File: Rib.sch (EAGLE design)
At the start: 34 parts, among them IC1 REG1117, IC2 REG1117, X1 JST-XH-03-PIN-LONG-PAD, X2 JST-XH-03-PIN-LONG-PAD

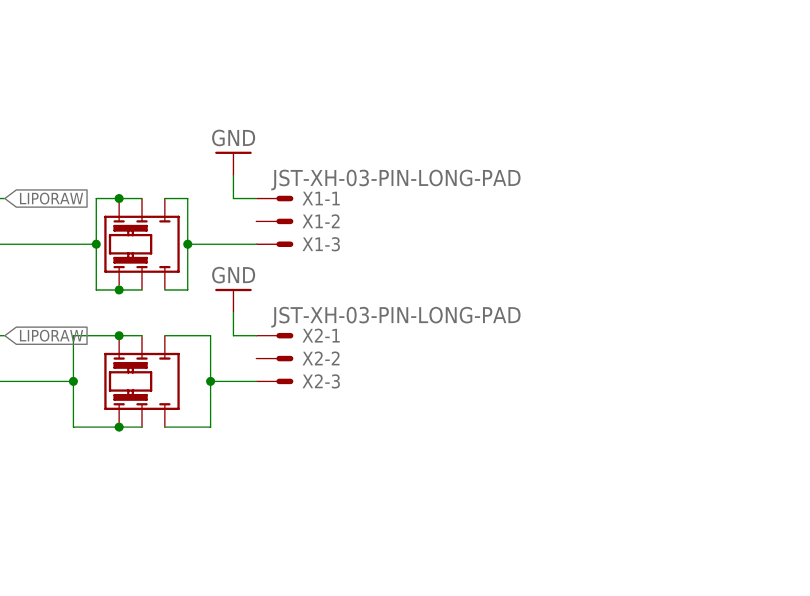
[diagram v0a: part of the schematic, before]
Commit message: Replaced JST power connectors with screw terminals
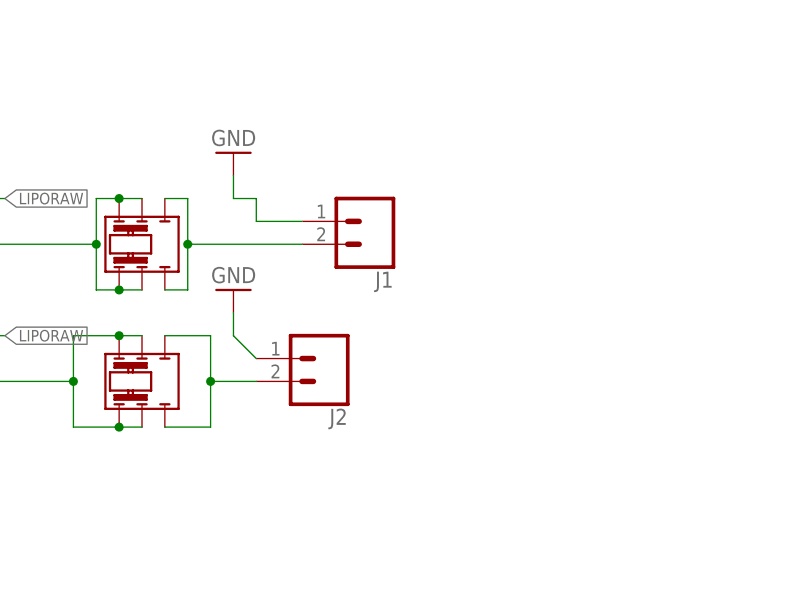
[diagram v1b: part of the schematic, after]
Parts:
- removed X1, X2: JST-XH-03-PIN-LONG-PAD, Rembrandt Electronics - JST XH Connectors v1-0:JST-XH-03-PIN-LONG-PAD
- added J1, J2: (no value), SparkFun-Connectors:CONN_023.5MM_LOCK
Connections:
- net GND: now also J1.1, J2.1; no longer X1-1.S, X2-1.S
- net N$11: now also J1.2; no longer X1-3.S
- net N$39: now also J2.2; no longer X2-3.S
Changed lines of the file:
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@@
 <part name="JP6" library="headers" deviceset="PINHD-1X19" device=""/>
 <part name="JP7" library="headers" deviceset="PINHD-1X19" device=""/>
-<part name="X1" library="Rembrandt Electronics - JST XH Connectors v1-0" deviceset="JST-XH-03-PIN" device="-LONG-PAD"/>
 <part name="JP2" library="headers" deviceset="PINHD-1X19" device=""/>
 <part name="JP8" library="headers" deviceset="PINHD-1X19" device=""/>
@@
 <part name="GND1" library="supply1" library_urn="urn:adsk.eagle:library:371" deviceset="GND" device=""/>
 <part name="GND2" library="supply1" library_urn="urn:adsk.eagle:library:371" deviceset="GND" device=""/>
-<part name="X2" library="Rembrandt Electronics - JST XH Connectors v1-0" deviceset="JST-XH-03-PIN" device="-LONG-PAD"/>
 <part name="U$3" library="wiichuck" deviceset="WIICHUCK" device=""/>
 <part name="U$5" library="wiichuck" deviceset="WIICHUCK" device=""/>
@@
 <part name="U$1" library="GF-126-0327" deviceset="DPDT" device=""/>
 <part name="U$2" library="GF-126-0327" deviceset="DPDT" device=""/>
+<part name="J1" library="SparkFun-Connectors" deviceset="CONN_02" device="3.5MM_LOCK"/>
+<part name="J2" library="SparkFun-Connectors" deviceset="CONN_02" device="3.5MM_LOCK"/>
 </parts>
 <sheets>
@@
 <instance part="JP6" gate="G$1" x="-55.88" y="-170.18"/>
 <instance part="JP7" gate="G$1" x="-35.56" y="-170.18"/>
-<instance part="X1" gate="-1" x="76.2" y="-55.88"/>
-<instance part="X1" gate="-2" x="76.2" y="-58.42"/>
-<instance part="X1" gate="-3" x="76.2" y="-60.96"/>
 <instance part="JP2" gate="G$1" x="-76.2" y="-170.18"/>
 <instance part="JP8" gate="G$1" x="-27.94" y="-170.18"/>
@@
 <instance part="GND1" gate="1" x="-35.56" y="-274.32"/>
 <instance part="GND2" gate="1" x="-22.86" y="-274.32"/>
-<instance part="X2" gate="-1" x="76.2" y="-71.12"/>
-<instance part="X2" gate="-2" x="76.2" y="-73.66"/>
-<instance part="X2" gate="-3" x="76.2" y="-76.2"/>
 <instance part="U$3" gate="G$1" x="38.1" y="-144.78"/>
 <instance part="U$5" gate="G$1" x="38.1" y="-180.34"/>
@@
 <instance part="U$1" gate="G$1" x="68.58" y="-53.34" rot="R90"/>
 <instance part="U$2" gate="G$1" x="68.58" y="-68.58" rot="R90"/>
+<instance part="J1" gate="G$1" x="86.36" y="-58.42" rot="R180"/>
+<instance part="J2" gate="G$1" x="81.28" y="-73.66" rot="R180"/>
 </instances>
 <busses>
@@
 <pinref part="GND10" gate="1" pin="GND"/>
 <wire x1="71.12" y1="-53.34" x2="71.12" y2="-55.88" width="0.1524" layer="91"/>
-<pinref part="X1" gate="-1" pin="S"/>
 <wire x1="71.12" y1="-55.88" x2="73.66" y2="-55.88" width="0.1524" layer="91"/>
+<pinref part="J1" gate="G$1" pin="1"/>
+<wire x1="78.74" y1="-58.42" x2="73.66" y2="-58.42" width="0.1524" layer="91"/>
+<wire x1="73.66" y1="-58.42" x2="73.66" y2="-55.88" width="0.1524" layer="91"/>
 </segment>
 <segment>
 <pinref part="GND9" gate="1" pin="GND"/>
 <wire x1="71.12" y1="-68.58" x2="71.12" y2="-71.12" width="0.1524" layer="91"/>
-<pinref part="X2" gate="-1" pin="S"/>
-<wire x1="71.12" y1="-71.12" x2="73.66" y2="-71.12" width="0.1524" layer="91"/>
+<wire x1="71.12" y1="-71.12" x2="73.66" y2="-73.66" width="0.1524" layer="91"/>
+<pinref part="J2" gate="G$1" pin="1"/>
 </segment>
 <segment>
@@
 <wire x1="66.04" y1="-66.04" x2="66.04" y2="-60.96" width="0.1524" layer="91"/>
 <wire x1="66.04" y1="-60.96" x2="66.04" y2="-55.88" width="0.1524" layer="91"/>
-<pinref part="X1" gate="-3" pin="S"/>
-<wire x1="73.66" y1="-60.96" x2="66.04" y2="-60.96" width="0.1524" layer="91"/>
+<wire x1="78.74" y1="-60.96" x2="66.04" y2="-60.96" width="0.1524" layer="91"/>
 <junction x="66.04" y="-60.96"/>
 <pinref part="U$1" gate="G$1" pin="C2"/>
@@
 <pinref part="U$1" gate="G$1" pin="C1"/>
 <wire x1="66.04" y1="-55.88" x2="63.5" y2="-55.88" width="0.1524" layer="91"/>
+<pinref part="J1" gate="G$1" pin="2"/>
 </segment>
 </net>
@@
 <wire x1="68.58" y1="-71.12" x2="68.58" y2="-76.2" width="0.1524" layer="91"/>
 <wire x1="68.58" y1="-76.2" x2="68.58" y2="-81.28" width="0.1524" layer="91"/>
-<pinref part="X2" gate="-3" pin="S"/>
 <wire x1="73.66" y1="-76.2" x2="68.58" y2="-76.2" width="0.1524" layer="91"/>
 <junction x="68.58" y="-76.2"/>
@@
 <pinref part="U$2" gate="G$1" pin="C1"/>
 <wire x1="63.5" y1="-71.12" x2="68.58" y2="-71.12" width="0.1524" layer="91"/>
-</segment>
-</net>
+<pinref part="J2" gate="G$1" pin="2"/>
+</segment>
+</net>

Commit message: ESP32 SDA now on pin 21
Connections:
- removed net N$38: JP17.14, JP7.14, JP8.14
- new net N$24: JP17.18, JP7.18, JP8.18
- net SDA: now also JP17.14, JP7.14, JP8.14; no longer JP17.18, JP7.18, JP8.18
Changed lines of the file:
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@@
-</segment>
-</net>
-<net name="N$38" class="0">
-<segment>
-<pinref part="JP8" gate="G$1" pin="14"/>
-<pinref part="JP17" gate="G$1" pin="14"/>
-<wire x1="-22.86" y1="-182.88" x2="-30.48" y2="-182.88" width="0.1524" layer="91"/>
-<pinref part="JP7" gate="G$1" pin="14"/>
-<junction x="-30.48" y="-182.88"/>
-<wire x1="-30.48" y1="-182.88" x2="-38.1" y2="-182.88" width="0.1524" layer="91"/>
 </segment>
 </net>
@@
 </segment>
 <segment>
-<pinref part="JP8" gate="G$1" pin="18"/>
-<pinref part="JP17" gate="G$1" pin="18"/>
-<wire x1="-22.86" y1="-193.04" x2="-30.48" y2="-193.04" width="0.1524" layer="91"/>
-<pinref part="JP7" gate="G$1" pin="18"/>
-<junction x="-30.48" y="-193.04"/>
-<wire x1="-30.48" y1="-193.04" x2="-38.1" y2="-193.04" width="0.1524" layer="91"/>
-</segment>
-<segment>
 <pinref part="JP14" gate="A" pin="9"/>
 <pinref part="JP20" gate="A" pin="9"/>
@@
 <wire x1="91.44" y1="-297.18" x2="81.28" y2="-297.18" width="0.1524" layer="91"/>
 <junction x="91.44" y="-297.18"/>
+</segment>
+<segment>
+<pinref part="JP8" gate="G$1" pin="14"/>
+<pinref part="JP17" gate="G$1" pin="14"/>
+<wire x1="-22.86" y1="-182.88" x2="-30.48" y2="-182.88" width="0.1524" layer="91"/>
+<pinref part="JP7" gate="G$1" pin="14"/>
+<junction x="-30.48" y="-182.88"/>
+<wire x1="-30.48" y1="-182.88" x2="-38.1" y2="-182.88" width="0.1524" layer="91"/>
 </segment>
 </net>
@@
 </segment>
 </net>
+<net name="N$24" class="0">
+<segment>
+<pinref part="JP17" gate="G$1" pin="18"/>
+<pinref part="JP8" gate="G$1" pin="18"/>
+<wire x1="-22.86" y1="-193.04" x2="-30.48" y2="-193.04" width="0.1524" layer="91"/>
+<pinref part="JP7" gate="G$1" pin="18"/>
+<wire x1="-30.48" y1="-193.04" x2="-38.1" y2="-193.04" width="0.1524" layer="91"/>
+<junction x="-30.48" y="-193.04"/>
+</segment>
+</net>

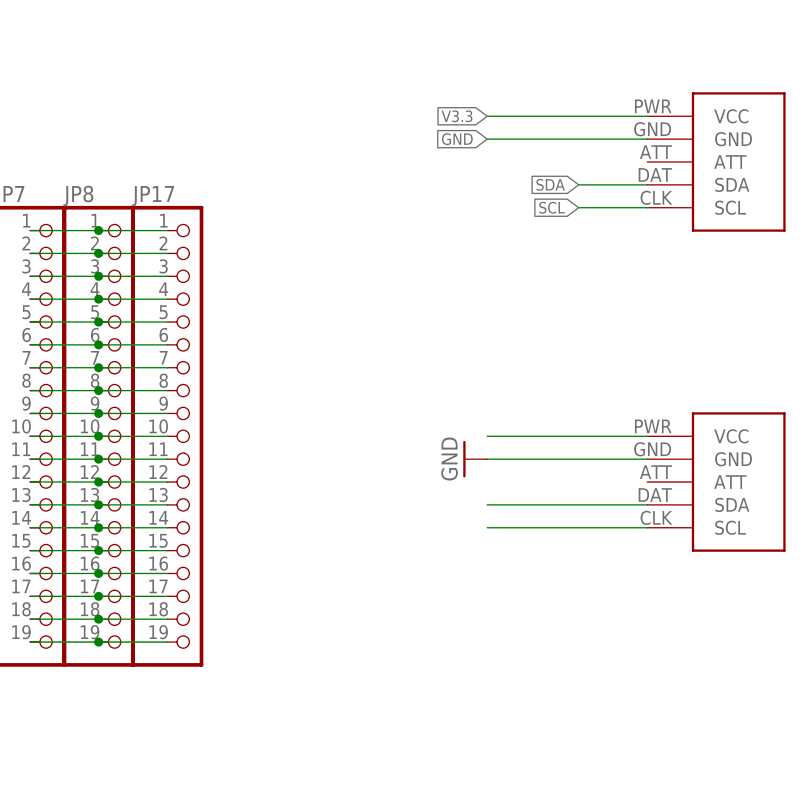
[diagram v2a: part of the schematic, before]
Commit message: DET pins routed to esp and teensy
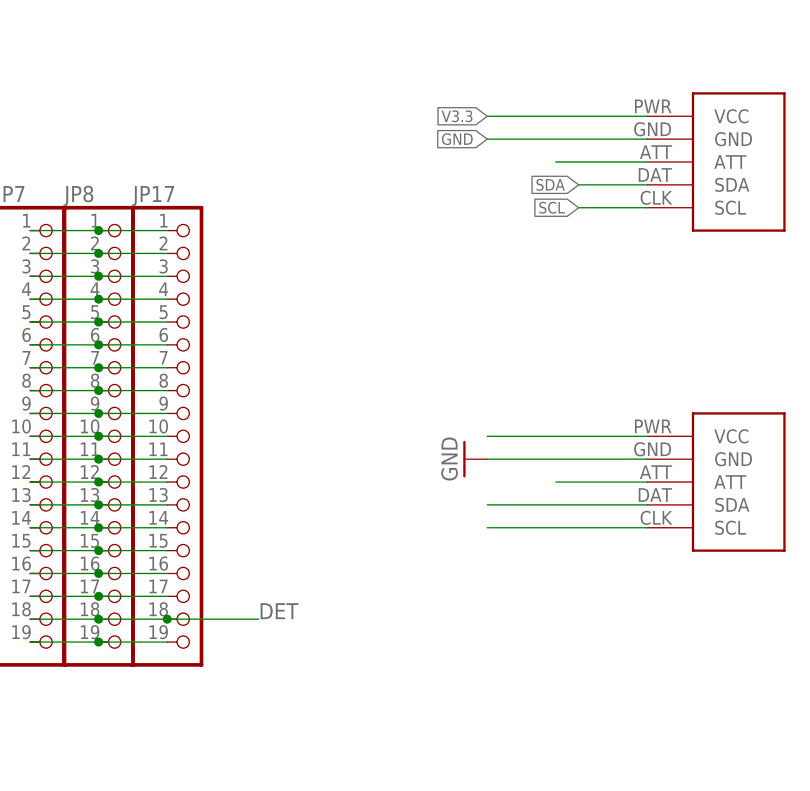
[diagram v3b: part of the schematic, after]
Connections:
- removed net N$107: JP12.24, JP21.24, JP9.24
- removed net N$24: JP17.18, JP7.18, JP8.18
- new net DET: JP12.24, JP17.18, JP21.24, JP7.18, JP8.18, JP9.24, U$3.ATT, U$5.ATT
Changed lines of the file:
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@@
 <?xml version="1.0" encoding="utf-8"?>
 <!DOCTYPE eagle SYSTEM "eagle.dtd">
-<eagle version="8.3.2">
+<eagle version="8.6.3">
 <drawing>
 <settings>
@@
 </segment>
 </net>
-<net name="N$107" class="0">
-<segment>
-<pinref part="JP9" gate="A" pin="24"/>
-<pinref part="JP21" gate="A" pin="24"/>
-<wire x1="119.38" y1="-335.28" x2="132.08" y2="-335.28" width="0.1524" layer="91"/>
-<pinref part="JP12" gate="A" pin="24"/>
-<wire x1="132.08" y1="-335.28" x2="139.7" y2="-335.28" width="0.1524" layer="91"/>
-<junction x="132.08" y="-335.28"/>
-</segment>
-</net>
 <net name="V3.3" class="0">
 <segment>
@@
 </segment>
 </net>
-<net name="N$24" class="0">
+<net name="DET" class="0">
 <segment>
 <pinref part="JP17" gate="G$1" pin="18"/>
@@
 <wire x1="-30.48" y1="-193.04" x2="-38.1" y2="-193.04" width="0.1524" layer="91"/>
 <junction x="-30.48" y="-193.04"/>
-</segment>
-</net>
+<wire x1="-22.86" y1="-193.04" x2="-12.7" y2="-193.04" width="0.1524" layer="91"/>
+<junction x="-22.86" y="-193.04"/>
+<label x="-12.7" y="-193.04" size="1.778" layer="95"/>
+</segment>
+<segment>
+<pinref part="U$3" gate="G$1" pin="ATT"/>
+<wire x1="30.48" y1="-142.24" x2="20.32" y2="-142.24" width="0.1524" layer="91"/>
+</segment>
+<segment>
+<pinref part="U$5" gate="G$1" pin="ATT"/>
+<wire x1="30.48" y1="-177.8" x2="20.32" y2="-177.8" width="0.1524" layer="91"/>
+</segment>
+<segment>
+<pinref part="JP9" gate="A" pin="24"/>
+<pinref part="JP21" gate="A" pin="24"/>
+<wire x1="119.38" y1="-335.28" x2="132.08" y2="-335.28" width="0.1524" layer="91"/>
+<pinref part="JP12" gate="A" pin="24"/>
+<wire x1="132.08" y1="-335.28" x2="139.7" y2="-335.28" width="0.1524" layer="91"/>
+<junction x="132.08" y="-335.28"/>
+</segment>
+</net>

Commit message: Replaced fuseholder with blade style automotive fuse
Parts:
- removed F1, F2: 0154, SMT_Fuse_0154001:0154
- added F3, F4: 3557-2, 3557-2:3557-2
- renumbered U$1 to SW1, U$2 to SW2
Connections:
- net LIPORAW: now also F3.P$2, F4.P$2; no longer F1.P$2, F2.P$2
- net VCC: now also F3.P$1, F4.P$1; no longer F1.P$1, F2.P$1
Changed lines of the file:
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@@
 <layer number="59" name="tCarbon" color="7" fill="1" visible="no" active="no"/>
 <layer number="60" name="bCarbon" color="7" fill="1" visible="no" active="no"/>
+<layer number="88" name="SimResults" color="9" fill="1" visible="yes" active="yes"/>
+<layer number="89" name="SimProbes" color="9" fill="1" visible="yes" active="yes"/>
 <layer number="90" name="Modules" color="5" fill="1" visible="yes" active="yes"/>
 <layer number="91" name="Nets" color="2" fill="1" visible="yes" active="yes"/>
@@
 <part name="GND7" library="supply1" library_urn="urn:adsk.eagle:library:371" deviceset="GND" device=""/>
 <part name="GND8" library="supply1" library_urn="urn:adsk.eagle:library:371" deviceset="GND" device=""/>
-<part name="F1" library="SMT_Fuse_0154001" deviceset="0154" device=""/>
-<part name="F2" library="SMT_Fuse_0154001" deviceset="0154" device=""/>
 <part name="GND9" library="supply1" library_urn="urn:adsk.eagle:library:371" deviceset="GND" device=""/>
 <part name="GND10" library="supply1" library_urn="urn:adsk.eagle:library:371" deviceset="GND" device=""/>
@@
 <part name="JP21" library="headers" deviceset="PINHD-1X24" device=""/>
 <part name="GND11" library="supply1" library_urn="urn:adsk.eagle:library:371" deviceset="GND" device=""/>
-<part name="U$1" library="GF-126-0327" deviceset="DPDT" device=""/>
-<part name="U$2" library="GF-126-0327" deviceset="DPDT" device=""/>
+<part name="SW1" library="GF-126-0327" deviceset="DPDT" device=""/>
+<part name="SW2" library="GF-126-0327" deviceset="DPDT" device=""/>
 <part name="J1" library="SparkFun-Connectors" deviceset="CONN_02" device="3.5MM_LOCK"/>
 <part name="J2" library="SparkFun-Connectors" deviceset="CONN_02" device="3.5MM_LOCK"/>
+<part name="F3" library="3557-2" deviceset="3557-2" device=""/>
+<part name="F4" library="3557-2" deviceset="3557-2" device=""/>
 </parts>
 <sheets>
@@
 <instance part="GND7" gate="1" x="238.76" y="-121.92"/>
 <instance part="GND8" gate="1" x="251.46" y="-121.92"/>
-<instance part="F1" gate="G$1" x="30.48" y="-53.34"/>
-<instance part="F2" gate="G$1" x="30.48" y="-68.58"/>
 <instance part="GND9" gate="1" x="71.12" y="-66.04" rot="R180"/>
 <instance part="GND10" gate="1" x="71.12" y="-50.8" rot="R180"/>
@@
 <instance part="JP21" gate="A" x="121.92" y="-304.8"/>
 <instance part="GND11" gate="1" x="10.16" y="-175.26" rot="R270"/>
-<instance part="U$1" gate="G$1" x="68.58" y="-53.34" rot="R90"/>
-<instance part="U$2" gate="G$1" x="68.58" y="-68.58" rot="R90"/>
+<instance part="SW1" gate="G$1" x="68.58" y="-53.34" rot="R90"/>
+<instance part="SW2" gate="G$1" x="68.58" y="-68.58" rot="R90"/>
 <instance part="J1" gate="G$1" x="86.36" y="-58.42" rot="R180"/>
 <instance part="J2" gate="G$1" x="81.28" y="-73.66" rot="R180"/>
+<instance part="F3" gate="G$1" x="30.48" y="-71.12"/>
+<instance part="F4" gate="G$1" x="30.48" y="-55.88"/>
 </instances>
 <busses>
@@
 </segment>
 <segment>
-<pinref part="F1" gate="G$1" pin="P$1"/>
 <wire x1="20.32" y1="-55.88" x2="12.7" y2="-55.88" width="0.1524" layer="91"/>
 <label x="12.7" y="-55.88" size="1.27" layer="95" rot="R180" xref="yes"/>
-</segment>
-<segment>
-<pinref part="F2" gate="G$1" pin="P$1"/>
+<pinref part="F4" gate="G$1" pin="P$1"/>
+</segment>
+<segment>
 <wire x1="20.32" y1="-71.12" x2="12.7" y2="-71.12" width="0.1524" layer="91"/>
 <label x="12.7" y="-71.12" size="1.27" layer="95" rot="R180" xref="yes"/>
+<pinref part="F3" gate="G$1" pin="P$1"/>
 </segment>
 <segment>
@@
 <net name="LIPORAW" class="0">
 <segment>
-<pinref part="F2" gate="G$1" pin="P$2"/>
 <wire x1="40.64" y1="-71.12" x2="43.18" y2="-71.12" width="0.1524" layer="91"/>
 <label x="45.72" y="-71.12" size="1.27" layer="95" xref="yes"/>
@@
 <wire x1="53.34" y1="-76.2" x2="43.18" y2="-76.2" width="0.1524" layer="91"/>
 <junction x="53.34" y="-76.2"/>
-<pinref part="U$2" gate="G$1" pin="A1"/>
+<pinref part="SW2" gate="G$1" pin="A1"/>
 <wire x1="53.34" y1="-71.12" x2="58.42" y2="-71.12" width="0.1524" layer="91"/>
-<pinref part="U$2" gate="G$1" pin="B1"/>
+<pinref part="SW2" gate="G$1" pin="B1"/>
 <wire x1="58.42" y1="-71.12" x2="60.96" y2="-71.12" width="0.1524" layer="91"/>
 <junction x="58.42" y="-71.12"/>
-<pinref part="U$2" gate="G$1" pin="A2"/>
+<pinref part="SW2" gate="G$1" pin="A2"/>
 <wire x1="53.34" y1="-81.28" x2="58.42" y2="-81.28" width="0.1524" layer="91"/>
-<pinref part="U$2" gate="G$1" pin="B2"/>
+<pinref part="SW2" gate="G$1" pin="B2"/>
 <wire x1="58.42" y1="-81.28" x2="60.96" y2="-81.28" width="0.1524" layer="91"/>
 <junction x="58.42" y="-81.28"/>
-</segment>
-<segment>
-<pinref part="F1" gate="G$1" pin="P$2"/>
+<pinref part="F3" gate="G$1" pin="P$2"/>
+</segment>
+<segment>
 <wire x1="40.64" y1="-55.88" x2="43.18" y2="-55.88" width="0.1524" layer="91"/>
 <label x="45.72" y="-55.88" size="1.27" layer="95" xref="yes"/>
@@
 <wire x1="43.18" y1="-60.96" x2="55.88" y2="-60.96" width="0.1524" layer="91"/>
 <junction x="55.88" y="-60.96"/>
-<pinref part="U$1" gate="G$1" pin="B1"/>
-<pinref part="U$1" gate="G$1" pin="A1"/>
+<pinref part="SW1" gate="G$1" pin="B1"/>
+<pinref part="SW1" gate="G$1" pin="A1"/>
 <wire x1="60.96" y1="-55.88" x2="58.42" y2="-55.88" width="0.1524" layer="91"/>
 <wire x1="58.42" y1="-55.88" x2="55.88" y2="-55.88" width="0.1524" layer="91"/>
 <junction x="58.42" y="-55.88"/>
-<pinref part="U$1" gate="G$1" pin="A2"/>
+<pinref part="SW1" gate="G$1" pin="A2"/>
 <wire x1="55.88" y1="-66.04" x2="58.42" y2="-66.04" width="0.1524" layer="91"/>
-<pinref part="U$1" gate="G$1" pin="B2"/>
+<pinref part="SW1" gate="G$1" pin="B2"/>
 <wire x1="58.42" y1="-66.04" x2="60.96" y2="-66.04" width="0.1524" layer="91"/>
 <junction x="58.42" y="-66.04"/>
+<pinref part="F4" gate="G$1" pin="P$2"/>
 </segment>
 </net>
@@
 <wire x1="78.74" y1="-60.96" x2="66.04" y2="-60.96" width="0.1524" layer="91"/>
 <junction x="66.04" y="-60.96"/>
-<pinref part="U$1" gate="G$1" pin="C2"/>
+<pinref part="SW1" gate="G$1" pin="C2"/>
 <wire x1="66.04" y1="-66.04" x2="63.5" y2="-66.04" width="0.1524" layer="91"/>
-<pinref part="U$1" gate="G$1" pin="C1"/>
+<pinref part="SW1" gate="G$1" pin="C1"/>
 <wire x1="66.04" y1="-55.88" x2="63.5" y2="-55.88" width="0.1524" layer="91"/>
 <pinref part="J1" gate="G$1" pin="2"/>
@@
 <wire x1="73.66" y1="-76.2" x2="68.58" y2="-76.2" width="0.1524" layer="91"/>
 <junction x="68.58" y="-76.2"/>
-<pinref part="U$2" gate="G$1" pin="C2"/>
+<pinref part="SW2" gate="G$1" pin="C2"/>
 <wire x1="63.5" y1="-81.28" x2="68.58" y2="-81.28" width="0.1524" layer="91"/>
-<pinref part="U$2" gate="G$1" pin="C1"/>
+<pinref part="SW2" gate="G$1" pin="C1"/>
 <wire x1="63.5" y1="-71.12" x2="68.58" y2="-71.12" width="0.1524" layer="91"/>
 <pinref part="J2" gate="G$1" pin="2"/>
